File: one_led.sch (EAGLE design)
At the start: 3 parts, among them U1_ WS2812B_LED

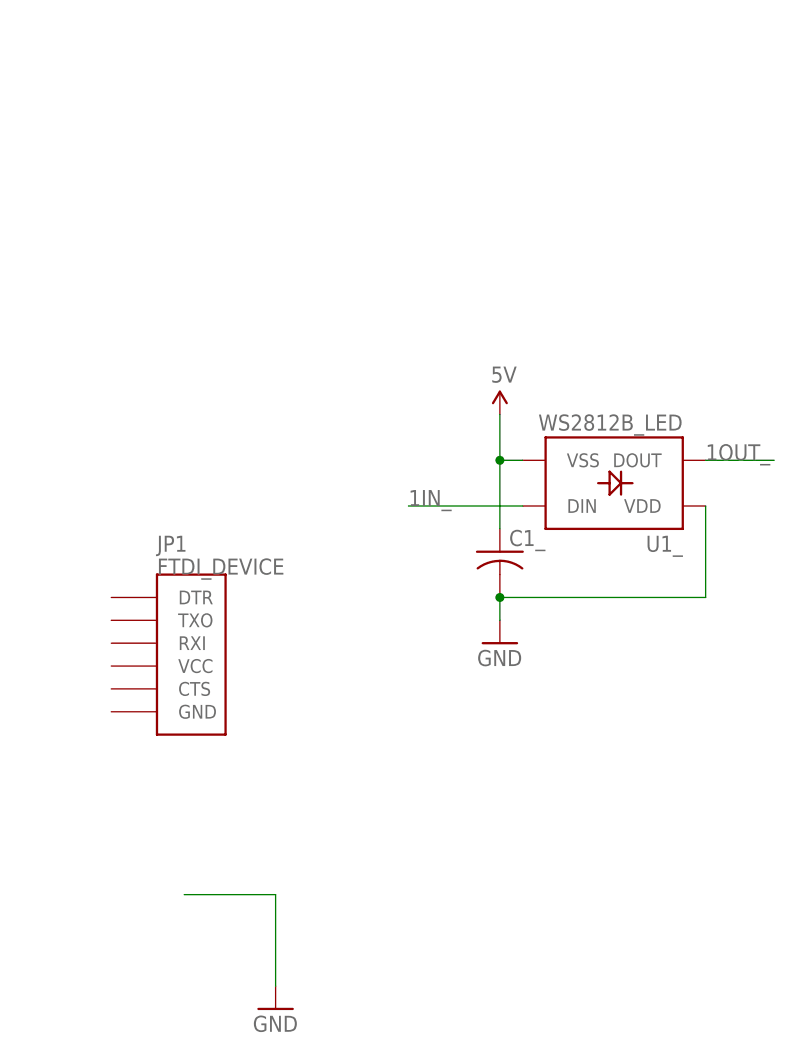
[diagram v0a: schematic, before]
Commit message: Bugfix: Automatically connect array inputs and outputs to any non-array parts that reference them.
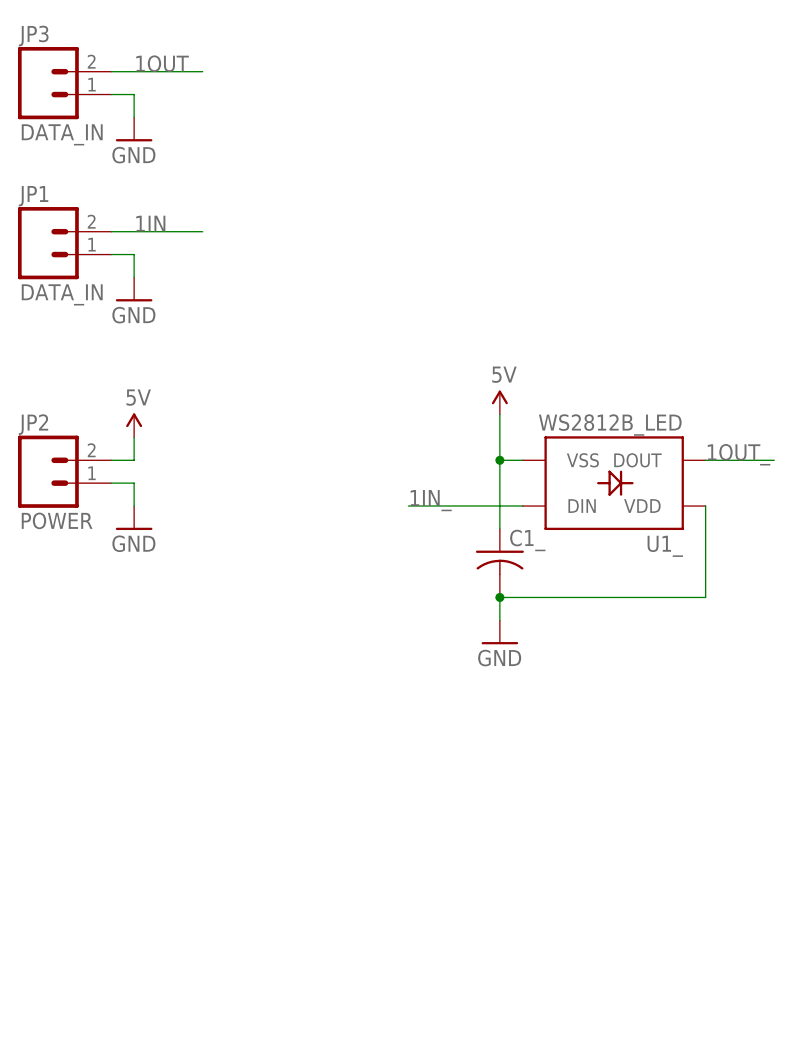
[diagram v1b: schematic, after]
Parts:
- added JP2: POWER, SparkFun-Connectors:M023.5MM_LOCK
- added JP3: DATA_IN, SparkFun-Connectors:M023.5MM_LOCK
- JP1: value FTDI_DEVICE -> DATA_IN; device SparkFun-Connectors:FTDI_DEVICE -> SparkFun-Connectors:M023.5MM_LOCK
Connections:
- new net 1IN: JP1.2
- new net 1OUT: JP3.2
- net 5V: now also JP2.2
- net GND: now also JP1.1, JP2.1, JP3.1
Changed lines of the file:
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@@
 <part name="U1_" library="blinkinlabs" deviceset="WS2812B_LED" device=""/>
 <part name="C1_" library="adafruit" deviceset="C-US" device="C0603K"/>
-<part name="SUPPLY_" library="SparkFun-Aesthetics" deviceset="5V" device=""/>
-<part name="GND_" library="SparkFun-Aesthetics" deviceset="GND" device=""/>
-<part name="JP1" library="SparkFun-Connectors" deviceset="FTDI_DEVICE" device=""/>
-<part name="GND1" library="SparkFun-Aesthetics" deviceset="GND" device=""/>
+<part name="SUPPLY1_" library="SparkFun-Aesthetics" deviceset="5V" device=""/>
+<part name="GND1_" library="SparkFun-Aesthetics" deviceset="GND" device=""/>
+<part name="JP1" library="SparkFun-Connectors" deviceset="M02" device="3.5MM_LOCK" value="DATA_IN"/>
+<part name="JP2" library="SparkFun-Connectors" deviceset="M02" device="3.5MM_LOCK" value="POWER"/>
+<part name="SUPPLY_1" library="SparkFun-Aesthetics" deviceset="5V" device=""/>
+<part name="GND_1" library="SparkFun-Aesthetics" deviceset="GND" device=""/>
+<part name="GND_2" library="SparkFun-Aesthetics" deviceset="GND" device=""/>
+<part name="JP3" library="SparkFun-Connectors" deviceset="M02" device="3.5MM_LOCK" value="DATA_IN"/>
+<part name="GND_3" library="SparkFun-Aesthetics" deviceset="GND" device=""/>
 </parts>
 <sheets>
@@
 <instance part="U1_" gate="G$1" x="30.48" y="66.04" rot="R180"/>
 <instance part="C1_" gate="G$1" x="17.78" y="58.42"/>
-<instance part="SUPPLY_" gate="G$1" x="17.78" y="73.66"/>
-<instance part="GND_" gate="1" x="17.78" y="48.26"/>
-<instance part="JP1" gate="G$1" x="-20.32" y="48.26"/>
-<instance part="GND1" gate="1" x="-7.14" y="7.62"/>
+<instance part="SUPPLY1_" gate="G$1" x="17.78" y="73.66"/>
+<instance part="GND1_" gate="1" x="17.78" y="48.26"/>
+<instance part="JP1" gate="G$1" x="-33.02" y="91.44"/>
+<instance part="JP2" gate="G$1" x="-33.02" y="66.04"/>
+<instance part="SUPPLY_1" gate="G$1" x="-22.86" y="71.12"/>
+<instance part="GND_1" gate="1" x="-22.86" y="60.96"/>
+<instance part="GND_2" gate="1" x="-22.86" y="86.36"/>
+<instance part="JP3" gate="G$1" x="-33.02" y="109.22"/>
+<instance part="GND_3" gate="1" x="-22.86" y="104.14"/>
 </instances>
 <busses>
@@
 <net name="5V" class="0">
 <segment>
-<pinref part="SUPPLY_" gate="G$1" pin="5V"/>
+<pinref part="SUPPLY1_" gate="G$1" pin="5V"/>
 <pinref part="U1_" gate="G$1" pin="VSS"/>
 <wire x1="17.78" y1="68.58" x2="20.32" y2="68.58" width="0.1524" layer="91"/>
@@
 <junction x="17.78" y="68.58"/>
 <wire x1="17.78" y1="68.58" x2="17.78" y2="73.66" width="0.1524" layer="91"/>
+</segment>
+<segment>
+<pinref part="JP2" gate="G$1" pin="2"/>
+<pinref part="SUPPLY_1" gate="G$1" pin="5V"/>
+<wire x1="-25.4" y1="68.58" x2="-22.86" y2="68.58" width="0.1524" layer="91"/>
+<wire x1="-22.86" y1="68.58" x2="-22.86" y2="71.12" width="0.1524" layer="91"/>
 </segment>
 </net>
@@
 <wire x1="17.78" y1="53.34" x2="17.78" y2="50.8" width="0.1524" layer="91"/>
 <junction x="17.78" y="53.34"/>
-<pinref part="GND_" gate="1" pin="GND"/>
+<pinref part="GND1_" gate="1" pin="GND"/>
 </segment>
 <segment>
-<pinref part="GND1" gate="1" pin="GND"/>
-<wire x1="-7.14" y1="10.16" x2="-7.14" y2="20.32" width="0.1524" layer="91"/>
-<wire x1="-7.14" y1="20.32" x2="-17.3" y2="20.32" width="0.1524" layer="91"/>
+<pinref part="JP1" gate="G$1" pin="1"/>
+<pinref part="GND_2" gate="1" pin="GND"/>
+<wire x1="-25.4" y1="91.44" x2="-22.86" y2="91.44" width="0.1524" layer="91"/>
+<wire x1="-22.86" y1="91.44" x2="-22.86" y2="88.9" width="0.1524" layer="91"/>
+</segment>
+<segment>
+<pinref part="JP2" gate="G$1" pin="1"/>
+<pinref part="GND_1" gate="1" pin="GND"/>
+<wire x1="-25.4" y1="66.04" x2="-22.86" y2="66.04" width="0.1524" layer="91"/>
+<wire x1="-22.86" y1="66.04" x2="-22.86" y2="63.5" width="0.1524" layer="91"/>
+</segment>
+<segment>
+<pinref part="JP3" gate="G$1" pin="1"/>
+<pinref part="GND_3" gate="1" pin="GND"/>
+<wire x1="-25.4" y1="109.22" x2="-22.86" y2="109.22" width="0.1524" layer="91"/>
+<wire x1="-22.86" y1="109.22" x2="-22.86" y2="106.68" width="0.1524" layer="91"/>
 </segment>
 </net>
+<net name="1IN" class="0">
+<segment>
+<pinref part="JP1" gate="G$1" pin="2"/>
+<wire x1="-25.4" y1="93.98" x2="-15.24" y2="93.98" width="0.1524" layer="91"/>
+<label x="-22.86" y="93.98" size="1.778" layer="95"/>
+</segment>
+</net>
+<net name="1OUT" class="0">
+<segment>
+<pinref part="JP3" gate="G$1" pin="2"/>
+<wire x1="-25.4" y1="111.76" x2="-15.24" y2="111.76" width="0.1524" layer="91"/>
+<label x="-22.86" y="111.76" size="1.778" layer="95"/>
+</segment>
+</net>
